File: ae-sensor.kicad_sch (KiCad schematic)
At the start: 18 parts, among them U1 ${SIM.PARAMS}, U2 ${SIM.PARAMS}

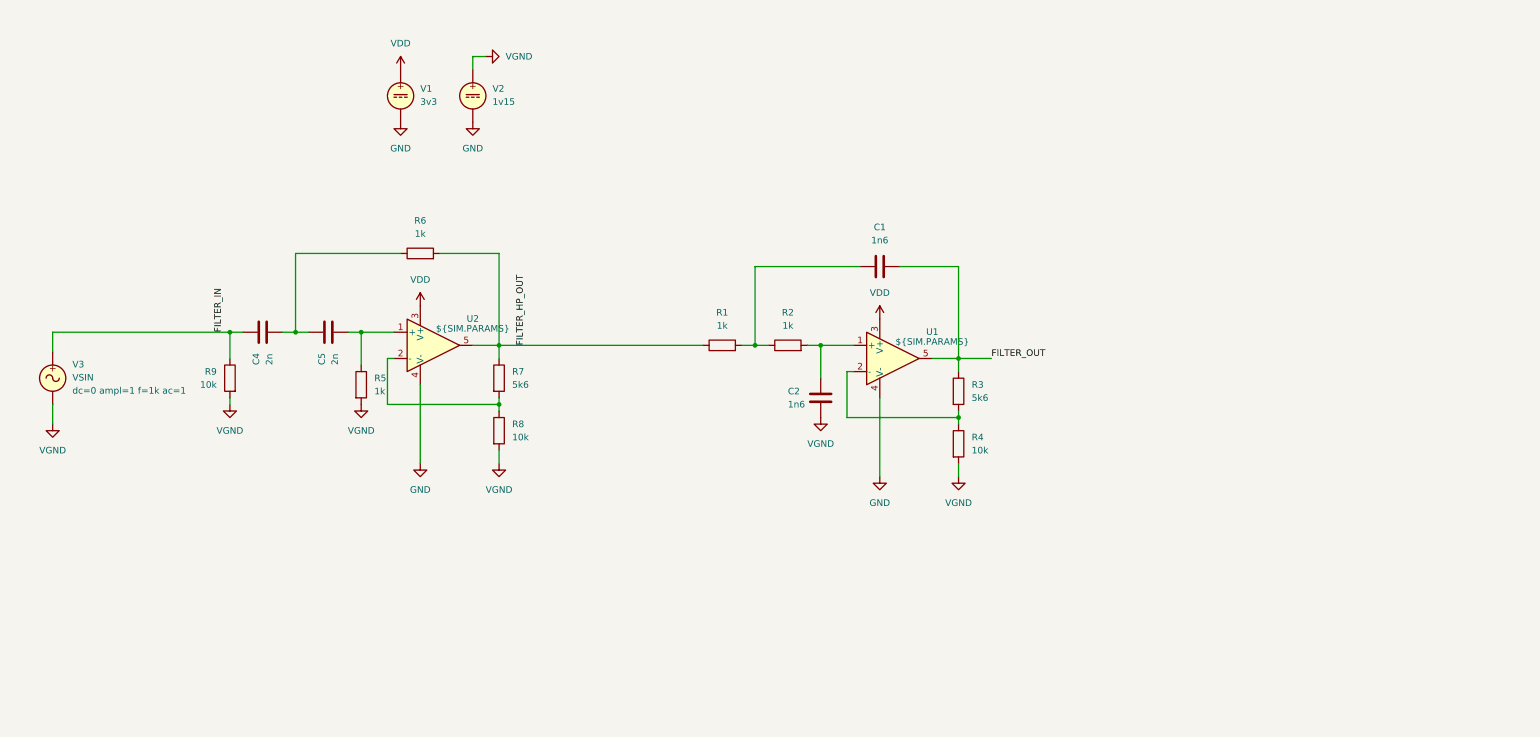
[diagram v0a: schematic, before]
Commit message: finalized filter tuning and OPAMP selection
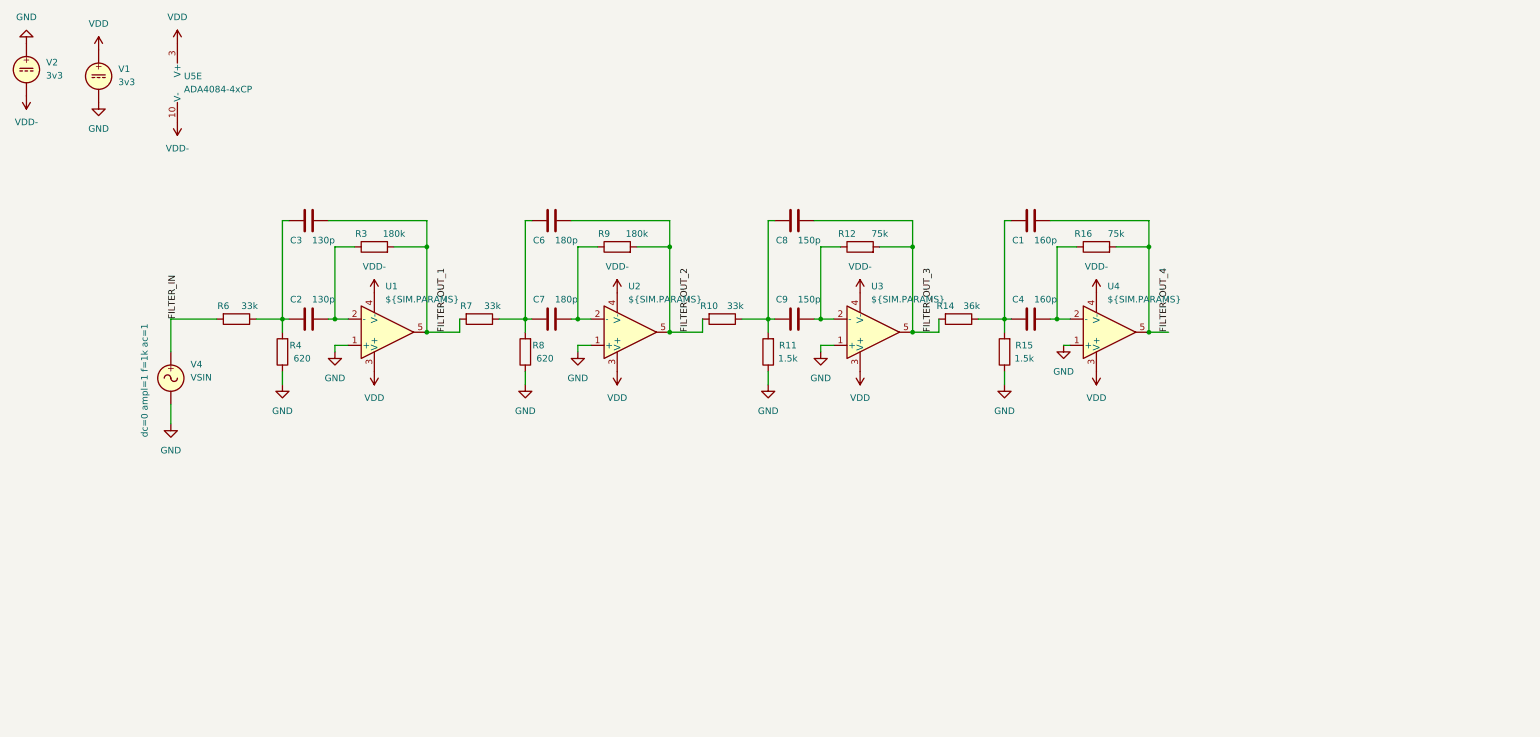
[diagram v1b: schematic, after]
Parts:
- removed C5: 2n, symbol Device:C
- removed R1, R2, R5: 1k, symbol Device:R
- removed V3: VSIN, symbol Simulation_SPICE:VSIN
- added C3: 130p, symbol Device:C
- added C6, C7: 180p, symbol Device:C
- added C8, C9: 150p, symbol Device:C
- added R10: 33k, symbol Device:R
- added R11, R15: 1.5k, symbol Device:R
- added R12, R16: 75k, symbol Device:R
- added R14: 36k, symbol Device:R
- added U3, U4: ${SIM.PARAMS}, symbol Simulation_SPICE:OPAMP
- added U5: ADA4084-4xCP, Package_CSP:LFCSP-16-1EP_4x4mm_P0.65mm_EP2.6x2.6mm, symbol Amplifier_Operational:ADA4084-4xCP
- added V4: VSIN, symbol Simulation_SPICE:VSIN
- C1: value 1n6 -> 160p
- C2: value 1n6 -> 130p
- C4: value 2n -> 160p
- R3: value 5k6 -> 180k
- R4, R8: value 10k -> 620
- R6: value 1k -> 33k
- R7: value 5k6 -> 33k
- R9: value 10k -> 180k
- V2: value 1v15 -> 3v3
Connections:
- net FILTER_IN: now also R6.2, V4.1; no longer C4.1, R9.1
- net GND: now also R4.1, R8.1, U1.1 (+), U2.1 (+), V2.1, R11.1, R15.1, U3.1 (+), U4.1 (+), V4.2; no longer U1.4 (V-), U2.4 (V-), V2.2
- net VDD: now also U3.3 (V+), U4.3 (V+), U5.3 (V+)
- net at R6.1: now also C2.1, R4.2, C3.1; no longer C4.2
- net at C1.1: now also C4.1, R14.1, R15.2
- removed net FILTER_HP_OUT: R6.2, R7.1, U2.5
- removed net FILTER_OUT: C1.2, R3.1, U1.5
- removed net VGND: C2.2, R4.2, R8.2, R9.2, V2.1
- new net: C2.2, R3.1, U1.2 (-)
- new net: C9.2, R12.1, U3.2 (-)
- new net: C8.1, C9.1, R10.1, R11.2
- new net: C4.2, R16.1, U4.2 (-)
- new net: C6.1, C7.1, R7.1, R8.2
- new net: C7.2, R9.1, U2.2 (-)
- new net FILTER_OUT_1: C3.2, R3.2, R7.2, U1.5
- new net FILTER_OUT_2: C6.2, R10.2, R9.2, U2.5
- new net FILTER_OUT_3: C8.2, R12.2, R14.2, U3.5
- new net FILTER_OUT_4: C1.2, R16.2, U4.5
- new net VDD-: U1.4 (V-), U2.4 (V-), U3.4 (V-), U4.4 (V-), U5.10 (V-), U5.17 (V-), V2.2
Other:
- moved on the sheet: V1

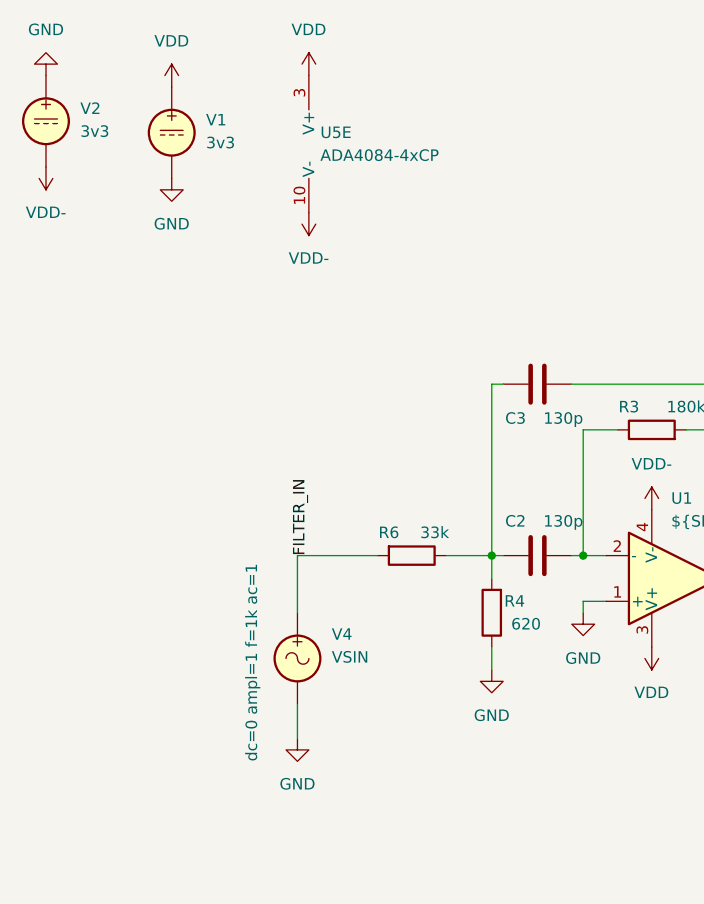
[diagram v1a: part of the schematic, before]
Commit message: added LTSpice simulation directory
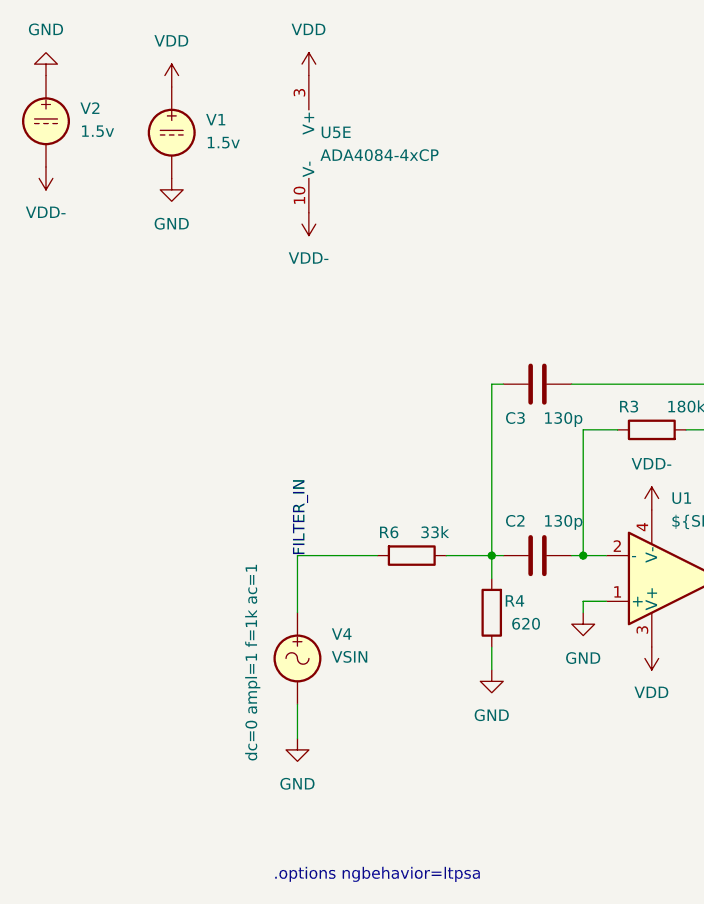
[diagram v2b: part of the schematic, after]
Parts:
- V1, V2: value 3v3 -> 1.5v
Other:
- note added: ".options ngbehavior=ltpsa"
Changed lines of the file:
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@@
 	(generator_version "9.0")
 	(paper "A4")
+	(text ".options ngbehavior=ltpsa"
+		(exclude_from_sim no)
+		(at 60.96 109.22 0)
+		(effects
+			(font
+				(size 1.27 1.27)
+			)
+		)
+	)
 	(junction
 		(at 148.59 76.2)
@@
 			)
 		)
-		(property "Value" "3v3"
+		(property "Value" "1.5v"
 			(at 41.91 27.8101 0)
 			(effects
@@
 			)
 		)
-		(property "Value" "3v3"
+		(property "Value" "1.5v"
 			(at 27.94 26.5401 0)
 			(effects

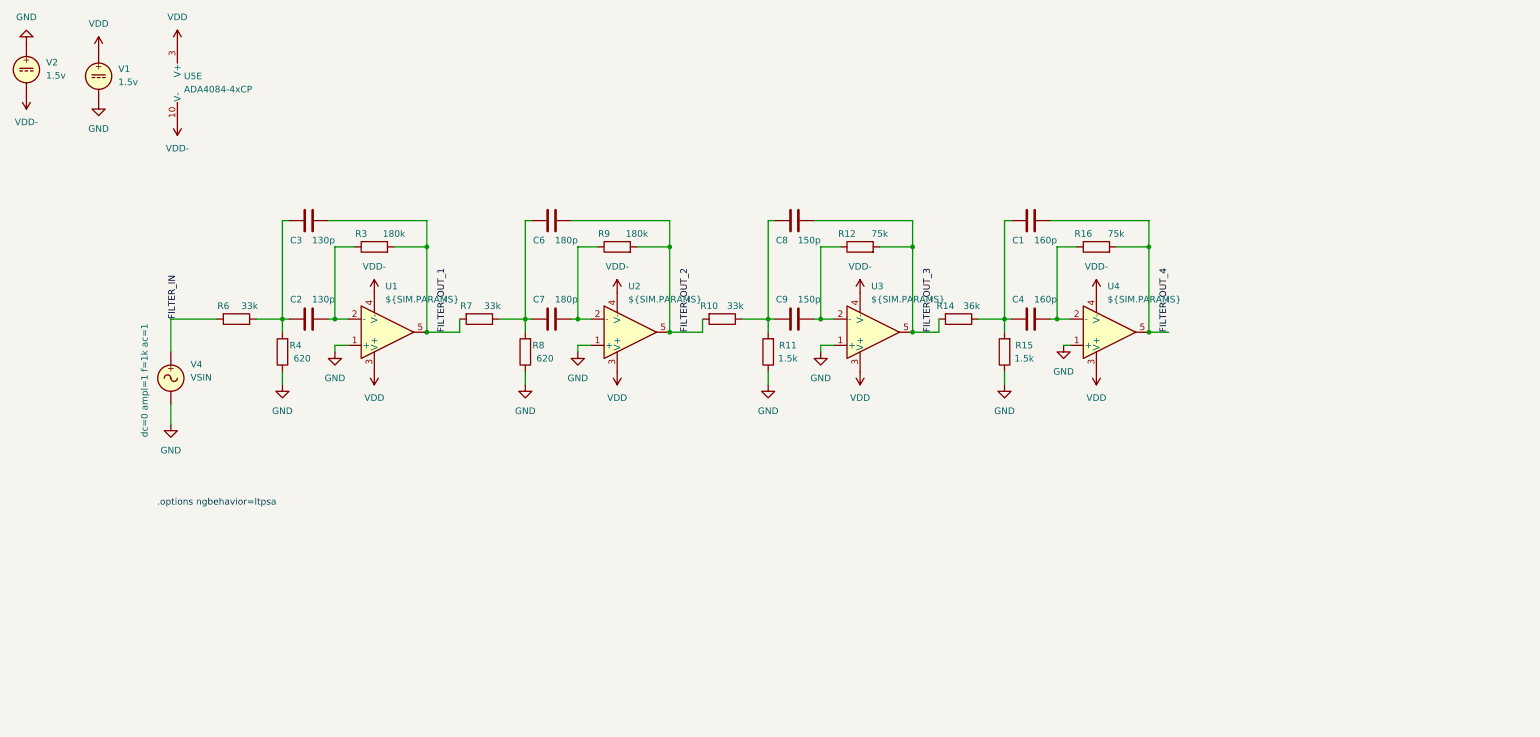
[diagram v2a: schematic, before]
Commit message: ultrasonic ae sensor power update
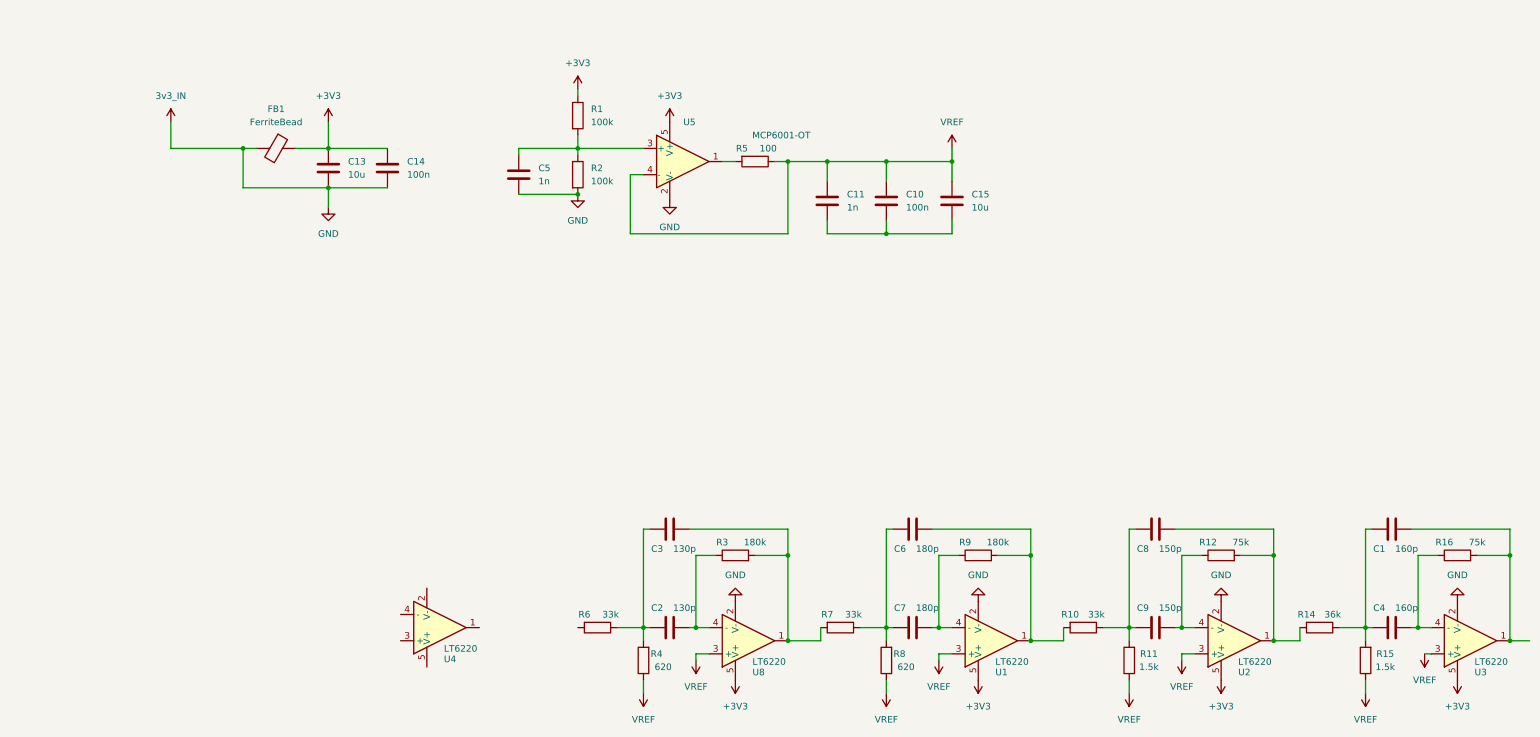
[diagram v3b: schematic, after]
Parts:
- removed U1, U2, U3, U4: ${SIM.PARAMS}, symbol Simulation_SPICE:OPAMP
- removed U5: ADA4084-4xCP, Package_CSP:LFCSP-16-1EP_4x4mm_P0.65mm_EP2.6x2.6mm, symbol Amplifier_Operational:ADA4084-4xCP
- removed V1, V2: 1.5v, symbol Simulation_SPICE:VDC
- removed V4: VSIN, symbol Simulation_SPICE:VSIN
- added C10, C14: 100n, Capacitor_SMD:C_0402_1005Metric_Pad0.74x0.62mm_HandSolder, symbol Device:C
- added C11, C5: 1n, Capacitor_SMD:C_0402_1005Metric_Pad0.74x0.62mm_HandSolder, symbol Device:C
- added C13, C15: 10u, Capacitor_SMD:C_0603_1608Metric, symbol Device:C
- added FB1: FerriteBead, Inductor_SMD:L_0603_1608Metric_Pad1.05x0.95mm_HandSolder, symbol Device:FerriteBead
- added R1, R2: 100k, Resistor_SMD:R_0402_1005Metric_Pad0.72x0.64mm_HandSolder, symbol Device:R
- added R5: 100, Resistor_SMD:R_0402_1005Metric_Pad0.72x0.64mm_HandSolder, symbol Device:R
- added U1, U2, U3, U4, U8: LT6220, ae_sensor_parts:TSOT-23-5_L2.9-W1.6-P0.95-LS2.8-BR, symbol ae_sensor_parts:LT6220IS5#TRMPBF
- added U5: MCP6001-OT, Package_TO_SOT_SMD:SOT-23-5, symbol Amplifier_Operational:MCP6001-OT
- C1, C2, C3, C4, C6, C7, C8, C9: footprint (none) -> Capacitor_SMD:C_0402_1005Metric_Pad0.74x0.62mm_HandSolder
- R10, R11, R12, R14, R15, R16, R3, R4, R6, R7, R8, R9: footprint (none) -> Resistor_SMD:R_0402_1005Metric_Pad0.72x0.64mm_HandSolder
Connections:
- net at C2.2, R3.1: now also U8.4 (-)
- net at C9.2, R12.1: now also U2.4 (-)
- net at C4.2, R16.1: now also U3.4 (-)
- net at C7.2, R9.1: now also U1.4 (-)
- net FILTER_IN: no longer names the net of R6.2
- net FILTER_OUT_1: no longer names the net of C3.2, R3.2, R7.2
- net FILTER_OUT_1: now also U8.1
- net FILTER_OUT_2: no longer names the net of C6.2, R10.2, R9.2
- net FILTER_OUT_2: now also U1.1
- net FILTER_OUT_3: no longer names the net of C8.2, R12.2, R14.2
- net FILTER_OUT_3: now also U2.1
- net FILTER_OUT_4: no longer names the net of C1.2, R16.2
- net FILTER_OUT_4: now also U3.1
- net GND renamed VREF
- net VREF: now also C10.1, C11.1, C15.1, R5.1, U1.3 (+), U2.3 (+), U3.3 (+), U5.4 (-), U8.3 (+)
- new net: C5.1, R1.2, R2.1, U5.3 (+)
- new net: R5.2, U5.1
- new net: C10.2, C11.2, C15.2
- new net +3V3: C13.1, C14.1, FB1.1, R1.1, U1.5 (V+), U2.5 (V+), U3.5 (V+), U5.5 (V+), U8.5 (V+)
- new net 3v3_IN: C13.2, C14.2, C5.2, FB1.2, R2.2, U1.2 (V-), U2.2 (V-), U3.2 (V-), U5.2 (V-), U8.2 (V-)
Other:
- note removed: ".options ngbehavior=ltpsa"
- moved on the sheet: C1, C2, C3, C4, C6, C7, C8, C9, R10, R11, R12, R14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
